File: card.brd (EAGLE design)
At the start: 84.8 x 53.3 mm, 56 parts, among them IC3 LTC1992CMS8, IC4 LTC1992CMS8, SW1 SPST_TACT-EVQQ2, SW2 SPST_TACT-EVQQ2, SW3 SPST_TACT-EVQQ2, SW4 SPST_TACT-EVQQ2

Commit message: Added components values
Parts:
- C1, C2, C3: value (none) -> 1u
- C4, C6, C7, C8, C9: value (none) -> 100n
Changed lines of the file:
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@@
 <setting verticaltext="up"/>
 </settings>
-<grid distance="0.025" unitdist="inch" unit="inch" style="lines" multiple="1" display="no" altdistance="0.0125" altunitdist="inch" altunit="inch"/>
+<grid distance="0.025" unitdist="inch" unit="mm" style="lines" multiple="1" display="no" altdistance="0.0125" altunitdist="inch" altunit="inch"/>
 <layers>
 <layer number="1" name="Top" color="4" fill="1" visible="yes" active="yes"/>
@@
 <element name="R3" library="resistor" package="M0805" value="" x="76.835" y="19.685" rot="MR270"/>
 <element name="R4" library="resistor" package="M0805" value="" x="76.835" y="33.655" rot="MR270"/>
-<element name="C1" library="resistor" package="C0805" value="" x="57.785" y="47.3075"/>
+<element name="C1" library="resistor" package="C0805" value="1u" x="57.785" y="47.3075"/>
 <element name="G1" library="battery" package="B2430UNI" value="B2430UNI" x="27.305" y="35.56"/>
 <element name="SW1" library="adafruit" package="EVQ-Q2" value="SPST_TACT-EVQQ2" x="43.815" y="5.08" smashed="yes" rot="R180">
@@
 <element name="R7" library="resistor" package="M0805" value="10k" x="6.35" y="27.305" rot="R90"/>
 <element name="R8" library="resistor" package="M0805" value="10k" x="6.35" y="31.75" rot="R90"/>
-<element name="C2" library="resistor" package="C0805" value="" x="12.065" y="24.13"/>
+<element name="C2" library="resistor" package="C0805" value="1u" x="12.065" y="24.13"/>
 <element name="R9" library="resistor" package="M0805" value="470k" x="7.62" y="41.275"/>
 <element name="R10" library="resistor" package="M0805" value="470k" x="12.065" y="41.275"/>
@@
 <element name="R16" library="resistor" package="M0805" value="10k" x="6.35" y="13.335" rot="MR270"/>
 <element name="R17" library="resistor" package="M0805" value="10k" x="6.35" y="17.78" rot="MR90"/>
-<element name="C3" library="resistor" package="C0805" value="" x="10.16" y="16.8275" rot="MR180"/>
+<element name="C3" library="resistor" package="C0805" value="1u" x="10.16" y="16.8275" rot="MR180"/>
 <element name="R18" library="resistor" package="M0805" value="470k" x="7.62" y="27.305" rot="MR180"/>
 <element name="R19" library="resistor" package="M0805" value="470k" x="12.065" y="27.305" rot="MR180"/>
@@
 </element>
 <element name="C5" library="adafruit" package="A/3216-18R" value="" x="12.7" y="19.05" rot="R270"/>
-<element name="C4" library="adafruit" package="C0805K" value="" x="16.8275" y="18.7325"/>
-<element name="C6" library="adafruit" package="C0805K" value="" x="23.8125" y="16.51" rot="MR270"/>
-<element name="C7" library="adafruit" package="C0805K" value="" x="22.225" y="6.985" rot="MR90"/>
-<element name="C8" library="adafruit" package="C0805K" value="" x="10.4775" y="12.065"/>
-<element name="C9" library="adafruit" package="C0805K" value="" x="10.795" y="25.0825" rot="MR180"/>
+<element name="C4" library="adafruit" package="C0805K" value="100n" x="16.8275" y="18.7325"/>
+<element name="C6" library="adafruit" package="C0805K" value="100n" x="23.8125" y="16.51" rot="MR270"/>
+<element name="C7" library="adafruit" package="C0805K" value="100n" x="22.225" y="6.985" rot="MR90"/>
+<element name="C8" library="adafruit" package="C0805K" value="100n" x="10.4775" y="12.065"/>
+<element name="C9" library="adafruit" package="C0805K" value="100n" x="10.795" y="25.0825" rot="MR180"/>
 <element name="J1" library="con-amp" package="10X03MTA" value="" x="4.7625" y="4.1275" rot="R180"/>
 <element name="J2" library="con-amp" package="10X03MTA" value="" x="13.0175" y="4.1275" rot="R180"/>

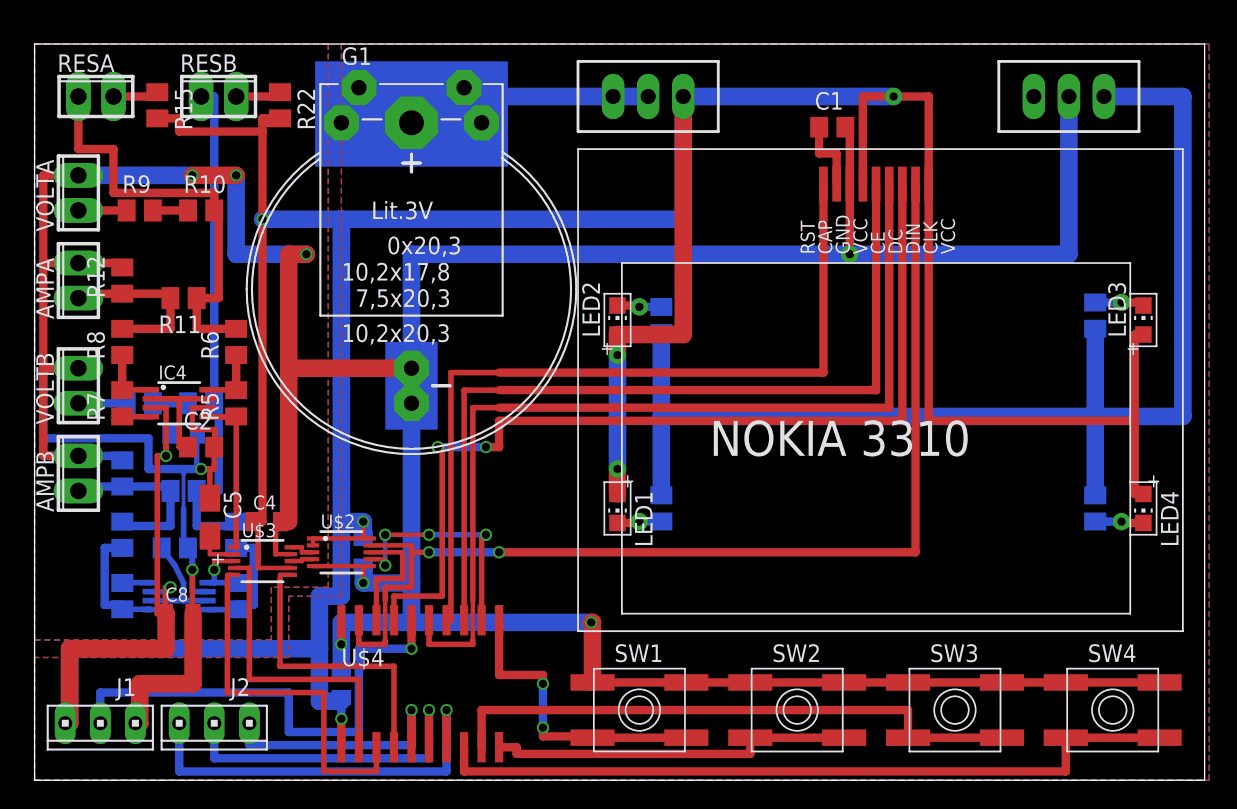
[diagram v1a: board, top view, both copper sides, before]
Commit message: Updated design and curved traces
Ready to ship !
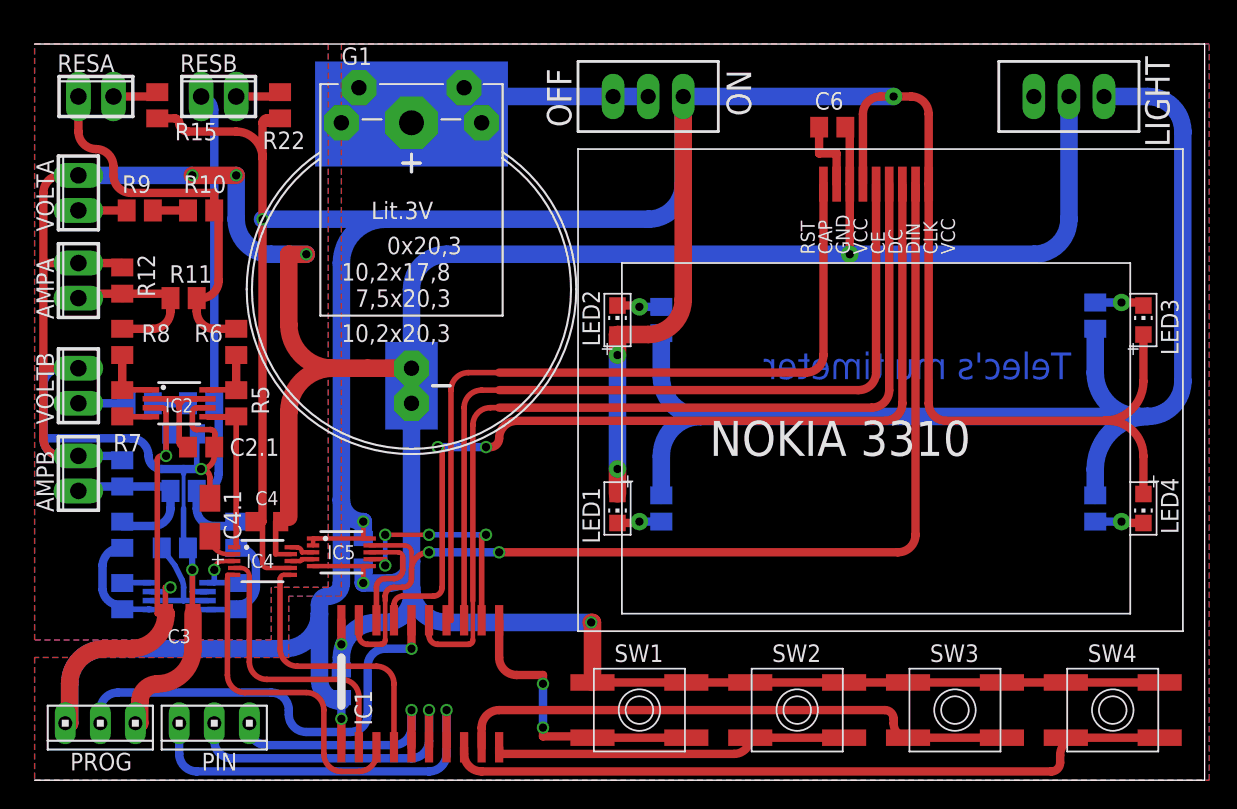
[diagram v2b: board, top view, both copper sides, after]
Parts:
- removed C7, C8, C9: 100n, adafruit:C0805K
- removed U$3: LTC6911CMS-1, HomeMade:MSOP10
- added C2.1, C3.1: 1u, resistor:C0805
- added C4.1: (no value), adafruit:A/3216-18R
- added IC2: LTC1992, linear-technology-2:MSOP8
- C1, C2, C3: value 1u -> 100n; device resistor:C0805 -> adafruit:C0805K
- C5: value (none) -> 100n; device adafruit:A/3216-18R -> adafruit:C0805K
- C6: value 100n -> 1u; device adafruit:C0805K -> resistor:C0805
- IC3: value LTC1992CMS8 -> LTC1992
- IC4: value LTC1992CMS8 -> LTC6911; device linear-technology-2:MSOP8 -> HomeMade:MSOP10
- IC5: value LTC2402CMS -> LTC2402
- moved C1 53.8 mm to (22.2, 6.99), flipped to the bottom, turned to 90 degrees
- moved C6 45.9 mm to (57.8, 47.3), flipped to the top, turned to 0 degrees
- moved IC4 12.9 mm to (16.5, 15.9)
- moved C5 11.4 mm to (23.8, 16.5), flipped to the bottom
- moved C3 4.77 mm to (10.5, 12.1), flipped to the top, turned to 0 degrees
- moved C2 1.59 mm to (10.8, 25.1), flipped to the bottom, turned to 180 degrees
- renumbered J1 to PROG, J2 to PIN, S1 to ON/OFF, S2 to LIGHT, U$2 to IC5, U$4 to IC1
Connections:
- net +3V3: now also C1.1, C2.1, C3.1, C5.1, IC2.3, IC4.7; no longer C6.1, C7.1, C8.1, C9.1, IC4.3, U$3.7
- net G0: now also IC4.4; no longer U$3.4
- net G1: now also IC4.5; no longer U$3.5
- net G2: now also IC4.6; no longer U$3.6
- net GND: now also C2.1.2, C3.1.2, C4.1.-, C5.2, IC2.6, IC4.9; no longer C5.-, C7.2, C8.2, C9.2, IC4.6, U$3.9
- net N$16: now also IC2.1; no longer IC4.1
- net N$17: now also IC2.8; no longer IC4.8
- net N$18: now also C4.1.+, IC4.2; no longer C5.+, U$3.2
- net N$19: now also IC2.4; no longer IC4.4
- net N$21: now also C2.1.1, IC2.2, IC2.7; no longer C2.1, IC4.2, IC4.7
- net N$29: now also IC4.8; no longer U$3.8
- net N$3: now also C6.1; no longer C1.1
- net N$31: now also C3.1.1; no longer C3.1
- net N$37: now also IC4.10; no longer U$3.10
- net RAWA: now also IC2.5, IC4.1; no longer IC4.5, U$3.1
- net RAWB: now also IC4.3; no longer U$3.3
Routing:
- net GND: track 338.8 -> 325.2 mm
- net +3V3: track 311.8 -> 301.5 mm
- net N$23: track 31.4 -> 27.7 mm
- net UPDI: track 35.7 -> 32.0 mm
- net G1: track 27.3 -> 24.3 mm
- net MOSI: track 69.1 -> 66.5 mm
- net D/C: track 68.4 -> 66.4 mm
- net N$33: track 37.5 -> 35.4 mm
- net N$21: track 8.24 -> 10.2 mm
- net G0: track 22.0 -> 20.2 mm
- net CLK: track 78.9 -> 77.1 mm
- net SW3: track 42.8 -> 41.1 mm
- net G2: track 21.5 -> 19.9 mm
- net N$8: track 18.6 -> 17.1 mm
- net RST: track 58.9 -> 57.4 mm
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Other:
- board text added: "LIGHT"
- board text added: "Max amp:"
- board text added: "Max volt:"
- board text added: "OFF"
- board text added: "ON"
- board text added: "Telec's multimeter"

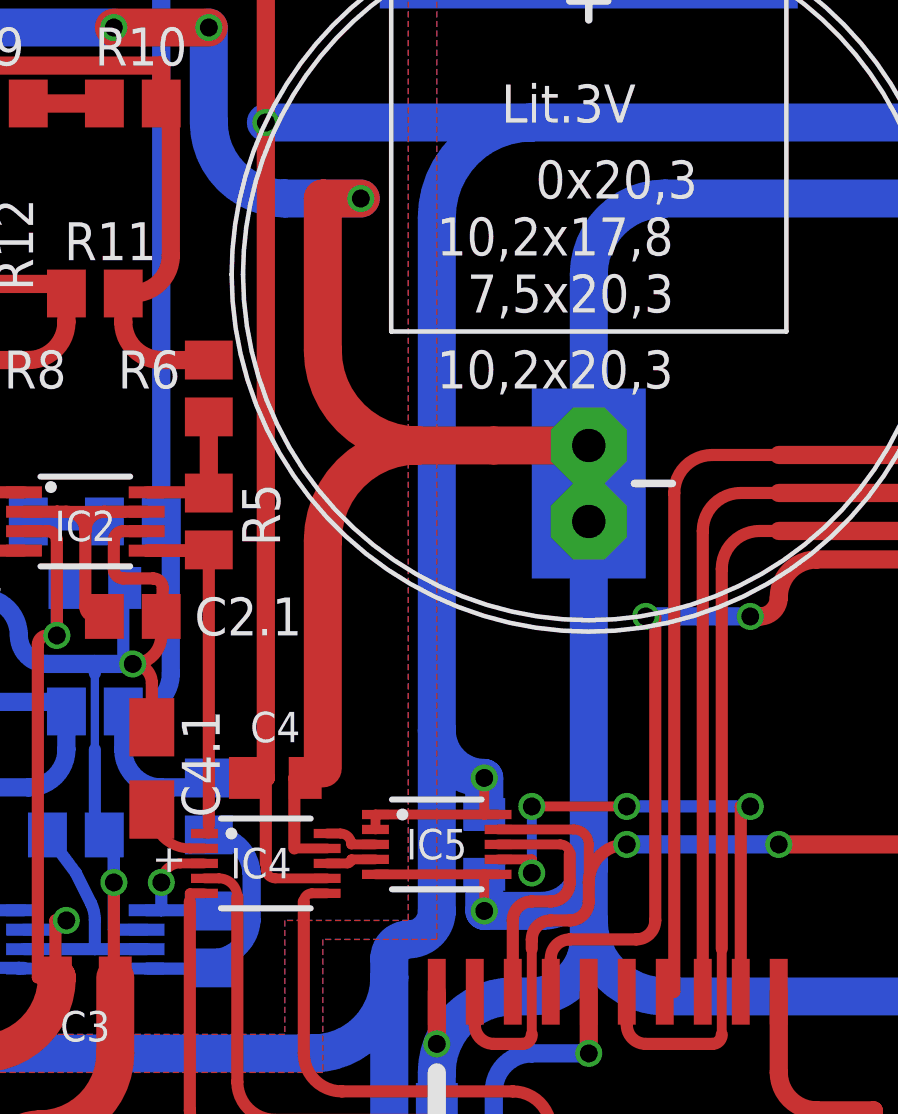
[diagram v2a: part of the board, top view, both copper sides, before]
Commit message: spaced a via
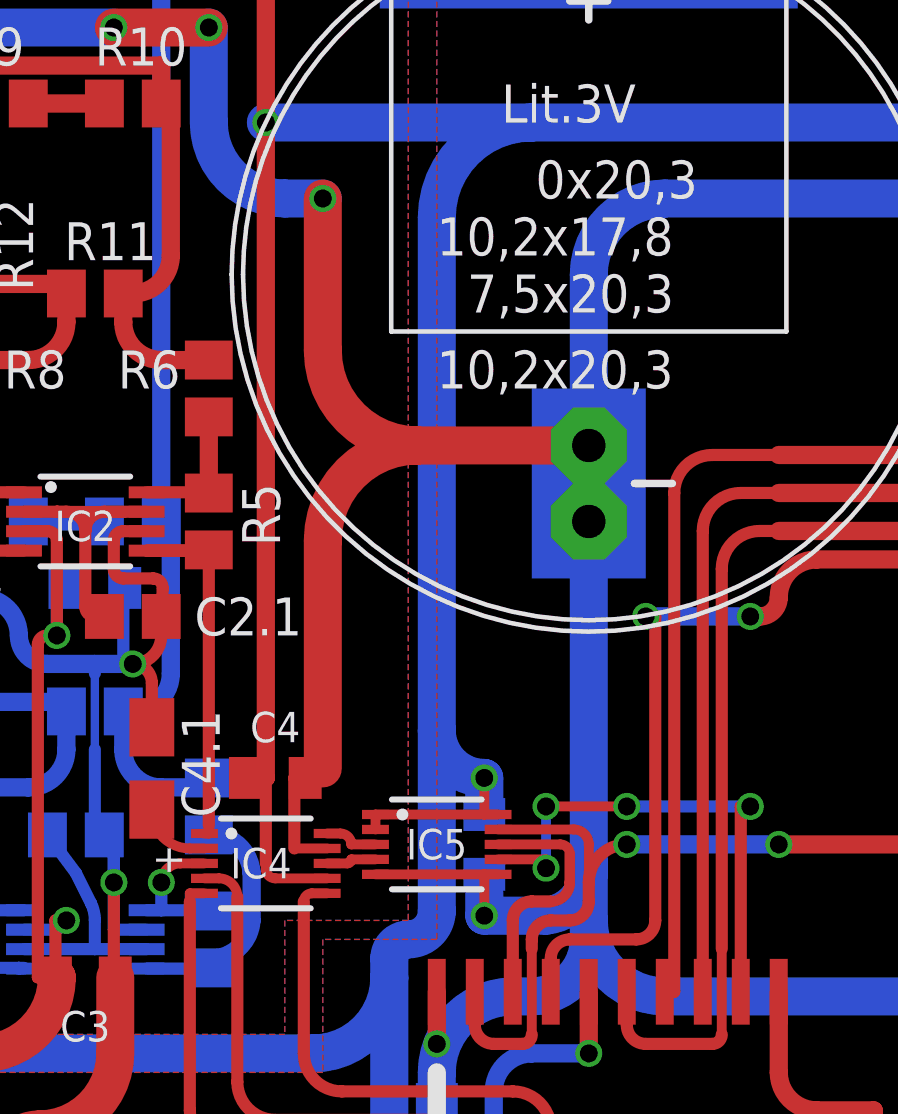
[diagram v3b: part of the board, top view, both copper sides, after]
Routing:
- net GND: track 325.2 -> 323.2 mm
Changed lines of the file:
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@@
 <wire x1="20.175" y1="15.51" x2="23.8125" y2="15.51" width="0.3302" layer="1"/>
 <wire x1="24.275" y1="15.51" x2="23.8125" y2="15.51" width="0.3302" layer="1"/>
-<wire x1="23.8125" y1="15.51" x2="23.8125" y2="14.2875" width="0.3302" layer="1"/>
-<via x="23.8125" y="14.2875" extent="1-16" drill="0.6" shape="square"/>
+<wire x1="23.8125" y1="15.51" x2="23.8125" y2="14.12875" width="0.3302" layer="1"/>
+<via x="23.8125" y="14.12875" extent="1-16" drill="0.6" shape="square"/>
 <wire x1="17.4625" y1="18.7325" x2="17.8275" y2="18.7325" width="0.4064" layer="1"/>
 <wire x1="27.305" y1="28.575" x2="27.305" y2="29.845" width="0.6096" layer="1"/>
@@
 <wire x1="14.605" y1="43.815" x2="14.605" y2="40.64" width="1.27" layer="16"/>
 <wire x1="14.605" y1="40.64" x2="17.145" y2="38.1" width="1.27" layer="16" curve="90"/>
-<wire x1="17.145" y1="38.1" x2="19.685" y2="38.1" width="1.27" layer="16"/>
+<wire x1="17.145" y1="38.1" x2="18.415" y2="38.1" width="1.27" layer="16"/>
 <via x="14.605" y="43.815" extent="1-16" drill="0.6" shape="square"/>
 <polygon width="0.4064" layer="1" isolate="0.4064">
@@
 <vertex x="0" y="0"/>
 </polygon>
-<wire x1="27.305" y1="29.845" x2="24.13" y2="29.845" width="1.27" layer="1"/>
+<wire x1="27.305" y1="29.845" x2="21.59" y2="29.845" width="1.27" layer="1"/>
 <wire x1="21.59" y1="29.845" x2="20.955" y2="29.845" width="1.27" layer="1"/>
-<via x="19.685" y="38.1" extent="1-16" drill="0.6" shape="square"/>
-<wire x1="19.685" y1="38.1" x2="18.415" y2="38.1" width="1.27" layer="1"/>
+<via x="18.415" y="38.1" extent="1-16" drill="0.6" shape="square"/>
 <wire x1="18.415" y1="18.7325" x2="17.8275" y2="18.7325" width="0.6096" layer="1"/>
-<wire x1="23.8125" y1="14.2875" x2="23.8125" y2="14.9225" width="1.27" layer="16"/>
+<wire x1="23.8125" y1="14.12875" x2="23.8125" y2="14.9225" width="1.27" layer="16"/>
 <wire x1="23.8125" y1="14.9225" x2="23.8125" y2="15.51" width="0.6096" layer="16"/>
 <wire x1="24.765" y1="11.43" x2="25.4" y2="11.43" width="1.27" layer="16"/>
@@
 <wire x1="40.3225" y1="11.43" x2="29.845" y2="11.43" width="1.27" layer="16"/>
 <wire x1="29.845" y1="11.43" x2="27.305" y2="13.97" width="1.27" layer="16" curve="-90"/>
-<wire x1="23.8125" y1="14.2875" x2="25.7175" y2="14.2875" width="1.27" layer="16"/>
-<wire x1="25.7175" y1="14.2875" x2="27.305" y2="15.875" width="1.27" layer="16" curve="90"/>
+<wire x1="23.8125" y1="14.12875" x2="25.87625" y2="14.12875" width="1.27" layer="16"/>
+<wire x1="25.87625" y1="14.12875" x2="27.305" y2="15.875" width="1.27" layer="16" curve="90"/>
 <wire x1="18.415" y1="38.1" x2="18.415" y2="33.02" width="1.27" layer="1"/>
 <wire x1="18.415" y1="33.02" x2="21.59" y2="29.845" width="1.27" layer="1" curve="90"/>
 <wire x1="18.415" y1="19.05" x2="18.415" y2="26.67" width="1.27" layer="1"/>
 <wire x1="18.415" y1="26.67" x2="21.59" y2="29.845" width="1.27" layer="1" curve="-90"/>
-<wire x1="21.59" y1="29.845" x2="24.13" y2="29.845" width="1.27" layer="1"/>
 </signal>
 <signal name="N$1">
@@
 <wire x1="24.765" y1="13.97" x2="25.4" y2="14.605" width="0.4064" layer="1" curve="-90"/>
 <wire x1="25.4" y1="14.605" x2="26.035" y2="14.605" width="0.4064" layer="1"/>
-<wire x1="26.035" y1="14.605" x2="26.67" y2="15.24" width="0.4064" layer="1" curve="90"/>
-<wire x1="26.67" y1="15.24" x2="26.67" y2="16.1925" width="0.4064" layer="1"/>
+<wire x1="26.035" y1="14.605" x2="26.67" y2="15.24" width="0.3556" layer="1" curve="90"/>
+<wire x1="26.67" y1="15.24" x2="26.67" y2="16.1925" width="0.3556" layer="1"/>
 </signal>
 <signal name="_CS_ADC">
 <contactref element="IC5" pad="7"/>
 <contactref element="IC1" pad="12"/>
-<wire x1="24.275" y1="16.01" x2="25.4" y2="16.01" width="0.3302" layer="1"/>
-<wire x1="25.4" y1="16.01" x2="25.4" y2="15.5575" width="0.3302" layer="1"/>
-<via x="25.4" y="15.5575" extent="1-16" drill="0.6" shape="square"/>
-<wire x1="25.4" y1="15.5575" x2="25.4" y2="17.78" width="0.3302" layer="16"/>
-<via x="25.4" y="17.78" extent="1-16" drill="0.6" shape="square"/>
-<wire x1="25.4" y1="17.78" x2="28.575" y2="17.78" width="0.3302" layer="1"/>
+<wire x1="24.275" y1="16.01" x2="25.87625" y2="16.01" width="0.3302" layer="1"/>
+<wire x1="25.87625" y1="16.01" x2="25.87625" y2="15.71625" width="0.3302" layer="1"/>
+<via x="25.87625" y="15.71625" extent="1-16" drill="0.6" shape="square"/>
+<wire x1="25.87625" y1="15.71625" x2="25.87625" y2="17.78" width="0.3302" layer="16"/>
+<via x="25.87625" y="17.78" extent="1-16" drill="0.6" shape="square"/>
+<wire x1="25.87625" y1="17.78" x2="28.575" y2="17.78" width="0.3302" layer="1"/>
 <wire x1="32.385" y1="11.585" x2="32.385" y2="17.78" width="0.4064" layer="1"/>
 <wire x1="32.385" y1="17.78" x2="32.7025" y2="17.78" width="0.4064" layer="1"/>

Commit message: Few changes, added logo
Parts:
- removed R1, R2: (no value), resistor:M0805
- removed R10, R9: 470k, resistor:M0805
- added R34: 1, resistor:M0805
- added R39: 100, resistor:M0805
- added R61, R62: 330, resistor:M0805
- C4.1: value (none) -> 1u
- R21: value 1 -> 470k
- R22: value 100 -> 470k
- R63, R64: value (none) -> 330
- moved R21 19.1 mm to (7.62, 41.3), flipped to the top, turned to 0 degrees
- moved R22 9.53 mm to (12.1, 41.3), turned to 0 degrees
- renumbered R11 to R23, R12 to R24, R13 to R36, R14 to R35, R15 to R29, R16 to R38, R17 to R37, R18 to R31, R19 to R32, R20 to R33, R3 to R64, R4 to R63, R5 to R26, R6 to R25, R7 to R28, R8 to R27
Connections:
- net +3V3: now also R39.2; no longer R22.2
- net GND: now also R34.2; no longer R21.2
- net LIGHT: now also R61.2, R62.1; no longer R1.2, R2.1
- net N$2: now also R61.1; no longer R1.1
- net N$22: now also R21.2, R22.1; no longer R10.1, R9.2
- net N$23: now also R22.2; no longer R10.2
- net N$27: now also R21.1; no longer R9.1
- net N$34: now also R34.1; no longer R21.1
- net N$36: now also R39.1; no longer R22.1
- net N$4: now also R62.2; no longer R2.2
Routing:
- net LIGHT: track 90.2 -> 88.8 mm
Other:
- board text added: "F:/Users/Loup/Doc/eagle/Logo/logoBW.bmp"
